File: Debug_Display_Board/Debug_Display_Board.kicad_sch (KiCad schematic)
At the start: 12 parts, among them SW1 SW_DIP_x08, U1 16V8B, U2 74HCT688, U8 74LVC1G07, X1 DIN41612_03x32_ABC_VMEbus

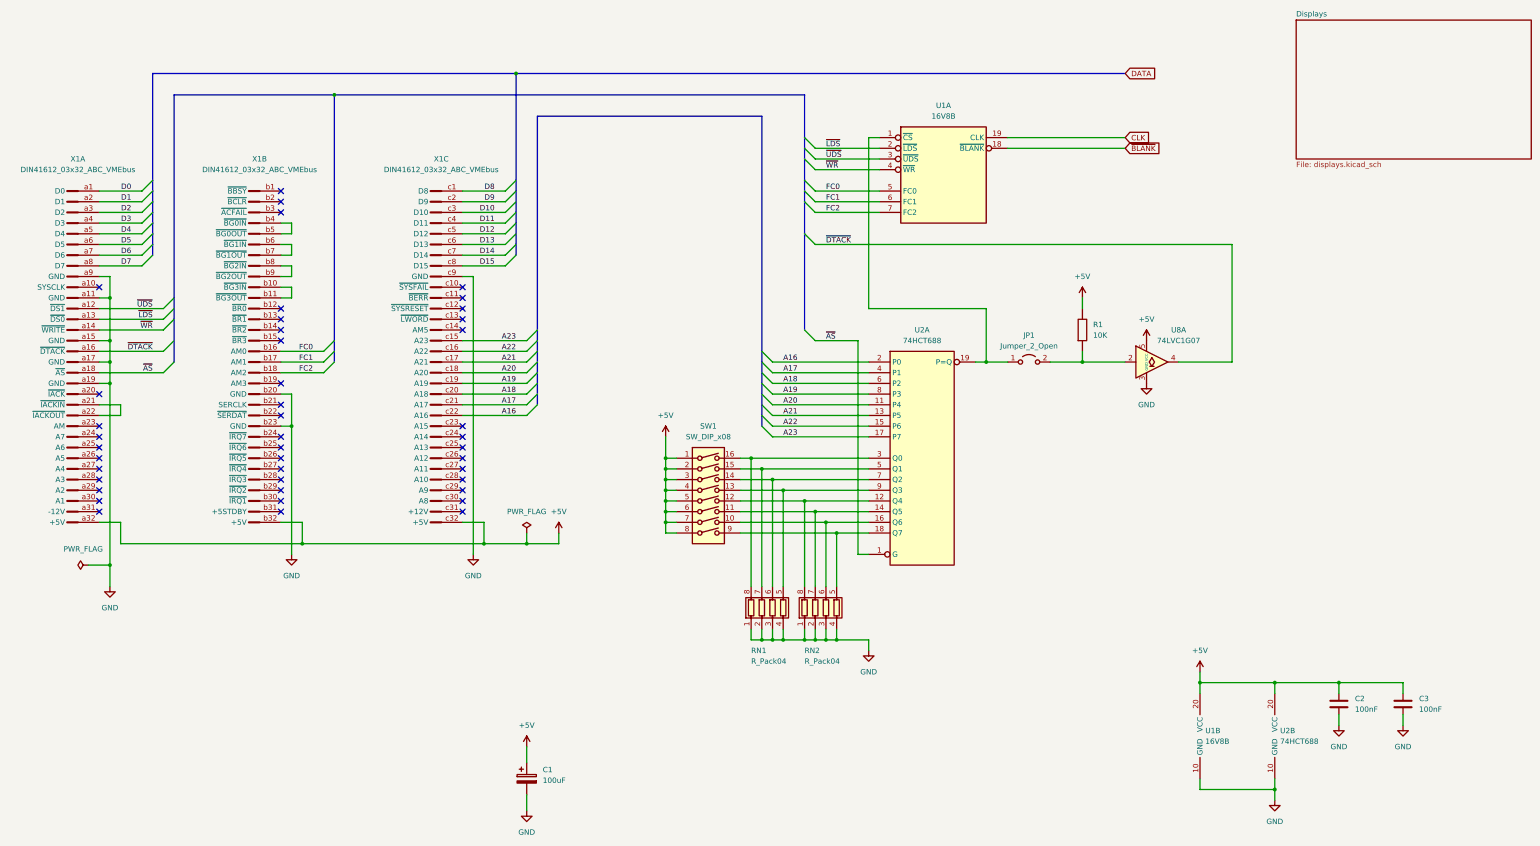
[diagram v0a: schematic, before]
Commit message: Resolve ERC failures
* Fix up bus names to resolve ERC failures
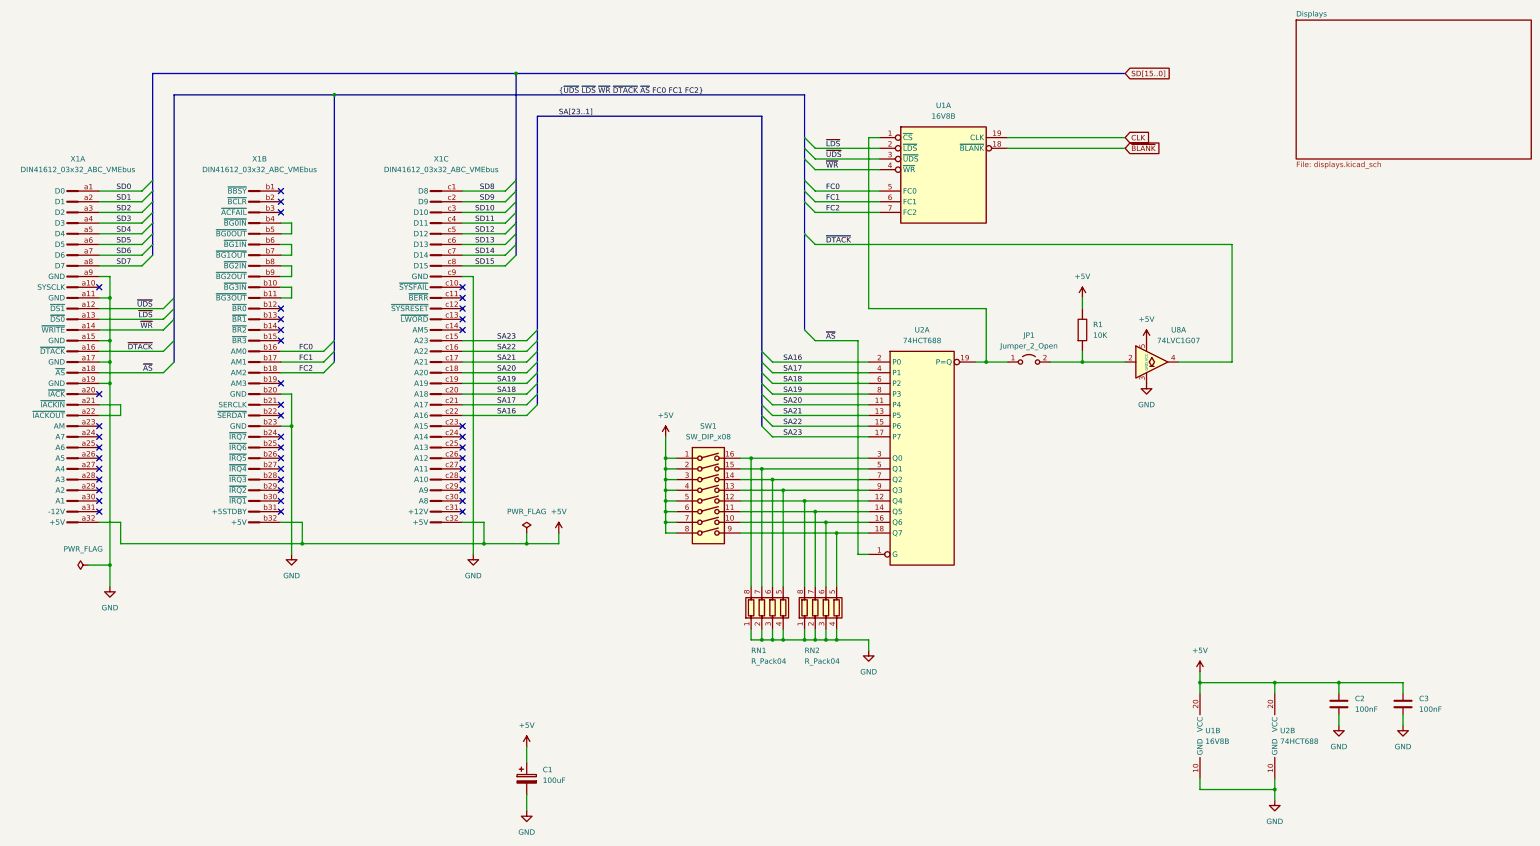
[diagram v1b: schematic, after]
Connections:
- net A16 renamed SA16
- net A17 renamed SA17
- net A18 renamed SA18
- net A19 renamed SA19
- net A20 renamed SA20
- net A21 renamed SA21
- net A22 renamed SA22
- net A23 renamed SA23
- net D0 renamed SD0
- net D1 renamed SD1
- net D10 renamed SD10
- net D11 renamed SD11
- net D12 renamed SD12
- net D13 renamed SD13
- net D14 renamed SD14
- net D15 renamed SD15
- net D2 renamed SD2
- net D3 renamed SD3
- net D4 renamed SD4
- net D5 renamed SD5
- net D6 renamed SD6
- net D7 renamed SD7
- net D8 renamed SD8
- net D9 renamed SD9
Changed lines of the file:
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@@
     (stroke (width 0) (type default) (color 0 0 0 0))
   )
-  (label "A16" (at 208.28 129.54 0)
+  (label "SA16" (at 208.28 129.54 0)
     (effects (font (size 1.27 1.27)) (justify left bottom))
   )
@@
     (effects (font (size 1.27 1.27)) (justify left bottom))
   )
-  (label "A17" (at 144.78 139.7 180)
-    (effects (font (size 1.27 1.27)) (justify right bottom))
-  )
-  (label "D13" (at 139.7 101.6 180)
+  (label "SA17" (at 144.78 139.7 180)
+    (effects (font (size 1.27 1.27)) (justify right bottom))
+  )
+  (label "SA[23..1]" (at 154.94 71.12 0)
+    (effects (font (size 1.27 1.27)) (justify left bottom))
+  )
+  (label "SD13" (at 139.7 101.6 180)
     (effects (font (size 1.27 1.27)) (justify right bottom))
   )
@@
     (effects (font (size 1.27 1.27)) (justify right bottom))
   )
-  (label "D12" (at 139.7 99.06 180)
-    (effects (font (size 1.27 1.27)) (justify right bottom))
-  )
-  (label "D4" (at 53.34 99.06 180)
+  (label "SD12" (at 139.7 99.06 180)
+    (effects (font (size 1.27 1.27)) (justify right bottom))
+  )
+  (label "SD4" (at 53.34 99.06 180)
     (effects (font (size 1.27 1.27)) (justify right bottom))
   )
@@
     (effects (font (size 1.27 1.27)) (justify left bottom))
   )
-  (label "D6" (at 53.34 104.14 180)
-    (effects (font (size 1.27 1.27)) (justify right bottom))
-  )
-  (label "A18" (at 144.78 137.16 180)
-    (effects (font (size 1.27 1.27)) (justify right bottom))
-  )
-  (label "A21" (at 144.78 129.54 180)
+  (label "SD6" (at 53.34 104.14 180)
+    (effects (font (size 1.27 1.27)) (justify right bottom))
+  )
+  (label "SA18" (at 144.78 137.16 180)
+    (effects (font (size 1.27 1.27)) (justify right bottom))
+  )
+  (label "SA21" (at 144.78 129.54 180)
     (effects (font (size 1.27 1.27)) (justify right bottom))
   )
@@
     (effects (font (size 1.27 1.27)) (justify right bottom))
   )
-  (label "D15" (at 139.7 106.68 180)
-    (effects (font (size 1.27 1.27)) (justify right bottom))
-  )
-  (label "A20" (at 208.28 139.7 0)
-    (effects (font (size 1.27 1.27)) (justify left bottom))
-  )
-  (label "D3" (at 53.34 96.52 180)
-    (effects (font (size 1.27 1.27)) (justify right bottom))
-  )
-  (label "A22" (at 144.78 127 180)
+  (label "SD15" (at 139.7 106.68 180)
+    (effects (font (size 1.27 1.27)) (justify right bottom))
+  )
+  (label "SA20" (at 208.28 139.7 0)
+    (effects (font (size 1.27 1.27)) (justify left bottom))
+  )
+  (label "SD3" (at 53.34 96.52 180)
+    (effects (font (size 1.27 1.27)) (justify right bottom))
+  )
+  (label "SA22" (at 144.78 127 180)
     (effects (font (size 1.27 1.27)) (justify right bottom))
   )
@@
     (effects (font (size 1.27 1.27)) (justify right bottom))
   )
-  (label "A23" (at 144.78 124.46 180)
-    (effects (font (size 1.27 1.27)) (justify right bottom))
-  )
-  (label "A18" (at 208.28 134.62 0)
-    (effects (font (size 1.27 1.27)) (justify left bottom))
-  )
-  (label "D7" (at 53.34 106.68 180)
-    (effects (font (size 1.27 1.27)) (justify right bottom))
-  )
-  (label "D9" (at 139.7 91.44 180)
-    (effects (font (size 1.27 1.27)) (justify right bottom))
-  )
-  (label "A23" (at 208.28 147.32 0)
+  (label "SA23" (at 144.78 124.46 180)
+    (effects (font (size 1.27 1.27)) (justify right bottom))
+  )
+  (label "SA18" (at 208.28 134.62 0)
+    (effects (font (size 1.27 1.27)) (justify left bottom))
+  )
+  (label "SD7" (at 53.34 106.68 180)
+    (effects (font (size 1.27 1.27)) (justify right bottom))
+  )
+  (label "SD9" (at 139.7 91.44 180)
+    (effects (font (size 1.27 1.27)) (justify right bottom))
+  )
+  (label "SA23" (at 208.28 147.32 0)
     (effects (font (size 1.27 1.27)) (justify left bottom))
   )
@@
     (effects (font (size 1.27 1.27)) (justify left bottom))
   )
-  (label "D5" (at 53.34 101.6 180)
+  (label "SD5" (at 53.34 101.6 180)
     (effects (font (size 1.27 1.27)) (justify right bottom))
   )
@@
     (effects (font (size 1.27 1.27)) (justify left bottom))
   )
-  (label "D1" (at 53.34 91.44 180)
+  (label "SD1" (at 53.34 91.44 180)
     (effects (font (size 1.27 1.27)) (justify right bottom))
   )
@@
     (effects (font (size 1.27 1.27)) (justify right bottom))
   )
-  (label "D0" (at 53.34 88.9 180)
-    (effects (font (size 1.27 1.27)) (justify right bottom))
-  )
-  (label "A20" (at 144.78 132.08 180)
-    (effects (font (size 1.27 1.27)) (justify right bottom))
-  )
-  (label "A21" (at 208.28 142.24 0)
-    (effects (font (size 1.27 1.27)) (justify left bottom))
-  )
-  (label "A19" (at 208.28 137.16 0)
+  (label "SD0" (at 53.34 88.9 180)
+    (effects (font (size 1.27 1.27)) (justify right bottom))
+  )
+  (label "SA20" (at 144.78 132.08 180)
+    (effects (font (size 1.27 1.27)) (justify right bottom))
+  )
+  (label "SA21" (at 208.28 142.24 0)
+    (effects (font (size 1.27 1.27)) (justify left bottom))
+  )
+  (label "SA19" (at 208.28 137.16 0)
     (effects (font (size 1.27 1.27)) (justify left bottom))
   )
@@
     (effects (font (size 1.27 1.27)) (justify left bottom))
   )
-  (label "D14" (at 139.7 104.14 180)
-    (effects (font (size 1.27 1.27)) (justify right bottom))
-  )
-  (label "D11" (at 139.7 96.52 180)
-    (effects (font (size 1.27 1.27)) (justify right bottom))
-  )
-  (label "A22" (at 208.28 144.78 0)
+  (label "SD14" (at 139.7 104.14 180)
+    (effects (font (size 1.27 1.27)) (justify right bottom))
+  )
+  (label "SD11" (at 139.7 96.52 180)
+    (effects (font (size 1.27 1.27)) (justify right bottom))
+  )
+  (label "SA22" (at 208.28 144.78 0)
     (effects (font (size 1.27 1.27)) (justify left bottom))
   )
@@
     (effects (font (size 1.27 1.27)) (justify right bottom))
   )
-  (label "A16" (at 144.78 142.24 180)
+  (label "SA16" (at 144.78 142.24 180)
     (effects (font (size 1.27 1.27)) (justify right bottom))
   )
@@
     (effects (font (size 1.27 1.27)) (justify left bottom))
   )
-  (label "D2" (at 53.34 93.98 180)
-    (effects (font (size 1.27 1.27)) (justify right bottom))
-  )
-  (label "A19" (at 144.78 134.62 180)
-    (effects (font (size 1.27 1.27)) (justify right bottom))
-  )
-  (label "A17" (at 208.28 132.08 0)
+  (label "SD2" (at 53.34 93.98 180)
+    (effects (font (size 1.27 1.27)) (justify right bottom))
+  )
+  (label "SA19" (at 144.78 134.62 180)
+    (effects (font (size 1.27 1.27)) (justify right bottom))
+  )
+  (label "SA17" (at 208.28 132.08 0)
+    (effects (font (size 1.27 1.27)) (justify left bottom))
+  )
+  (label "{~{UDS} ~{LDS} ~{WR} ~{DTACK} ~{AS} FC0 FC1 FC2}" (at 154.94 66.04 0)
     (effects (font (size 1.27 1.27)) (justify left bottom))
   )
@@
     (effects (font (size 1.27 1.27)) (justify left bottom))
   )
-  (label "D8" (at 139.7 88.9 180)
+  (label "SD8" (at 139.7 88.9 180)
     (effects (font (size 1.27 1.27)) (justify right bottom))
   )
@@
     (effects (font (size 1.27 1.27)) (justify right bottom))
   )
-  (label "D10" (at 139.7 93.98 180)
-    (effects (font (size 1.27 1.27)) (justify right bottom))
-  )
-  (global_label "DATA" (shape input) (at 289.56 60.96 0) (fields_autoplaced)
+  (label "SD10" (at 139.7 93.98 180)
+    (effects (font (size 1.27 1.27)) (justify right bottom))
+  )
+  (global_label "SD[15..0]" (shape input) (at 289.56 60.96 0) (fields_autoplaced)
     (effects (font (size 1.27 1.27)) (justify left))
-    (property "Intersheet References" "${INTERSHEET_REFS}" (id 0) (at 296.3879 60.8806 0)
+    (property "Intersheet References" "${INTERSHEET_REFS}" (id 0) (at 300.9841 60.8806 0)
       (effects (font (size 1.27 1.27)) (justify left) hide)
     )
@@
       (effects (font (size 1.27 1.27)) hide)
     )
+    (pin "1")
+    (pin "18")
     (pin "19")
     (pin "2")
@@
     (pin "6")
     (pin "7")
-    (pin "8")
     (pin "10")
     (pin "20")
@@
       (reference "#PWR016") (unit 1) (value "+5V") (footprint "")
     )
-    (path "/3a2cf847-1ce6-4ae0-a851-805df99b714e/e15e3129-835e-41cc-82c1-9ffbbbe53148"
-      (reference "#PWR017") (unit 1) (value "GND") (footprint "")
-    )
     (path "/3a2cf847-1ce6-4ae0-a851-805df99b714e/6259bb6e-eeb6-4e24-910d-dde9d9c667df"
